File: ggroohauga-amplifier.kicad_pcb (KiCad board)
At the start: 2 copper layers, 95 x 31 mm, 12 parts

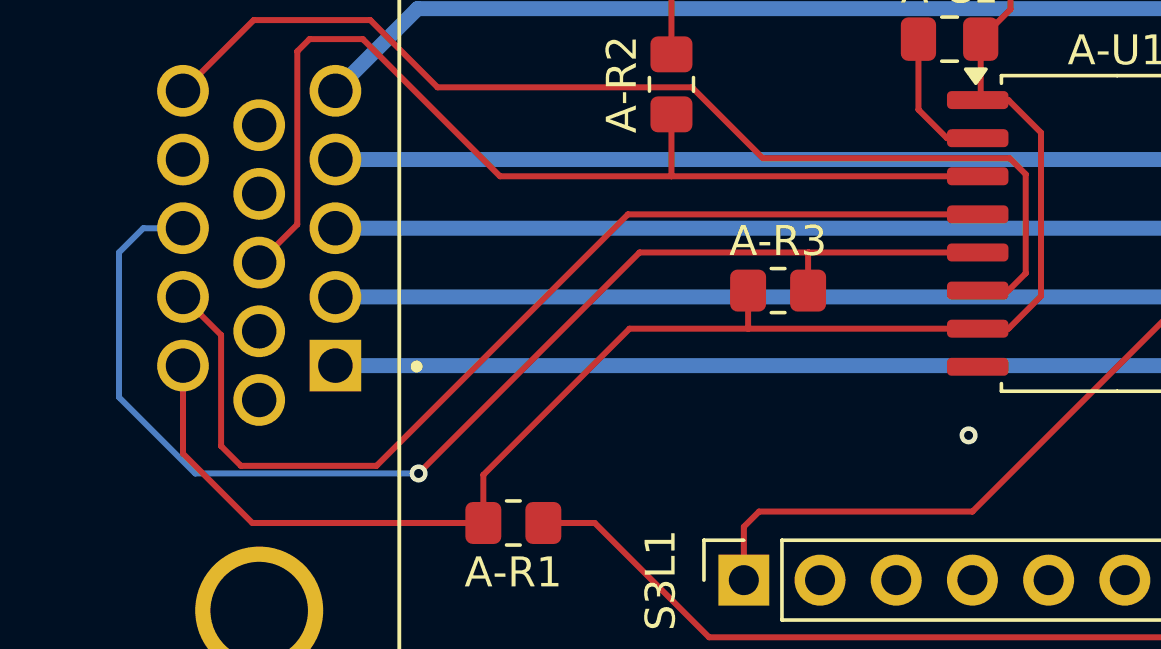
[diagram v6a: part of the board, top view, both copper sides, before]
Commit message: Move pull-up from AMP_RX to AMP_TX
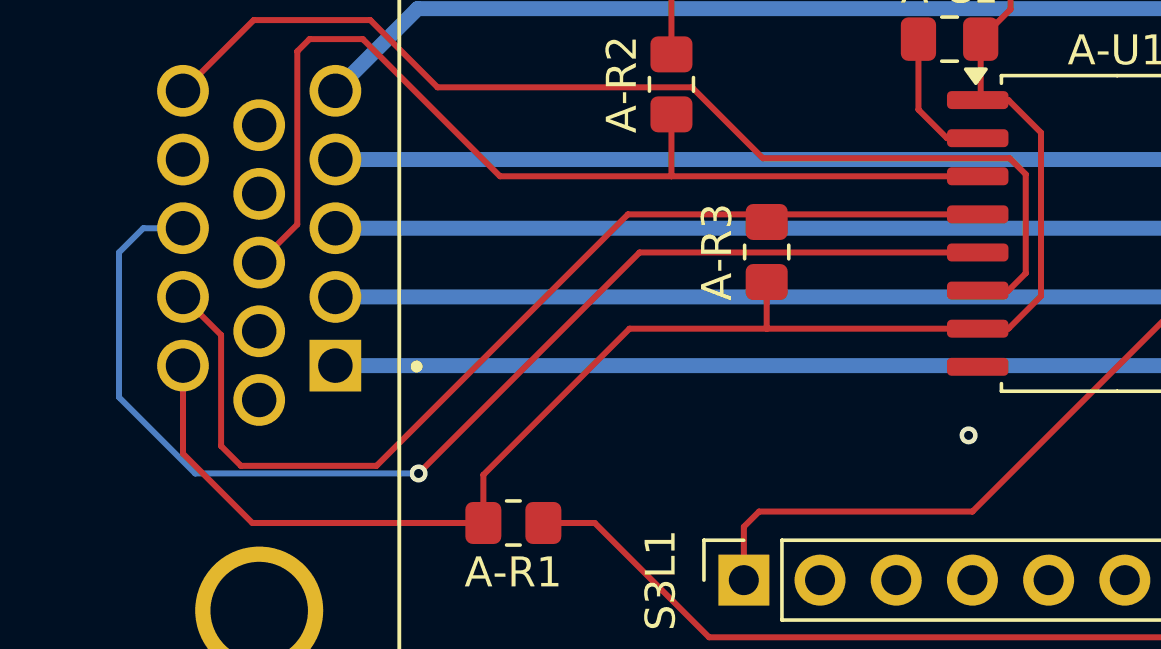
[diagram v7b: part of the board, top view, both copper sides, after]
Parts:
- moved A-R3 1.34 mm to (82.3, 66.5), turned to 90 degrees
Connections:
- A-R3 pad 2: /Common/AMP_RX -> /Common/AMP_TX
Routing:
- net /Common/AMP_RX: track 41.3 -> 40.0 mm
- net /Common/AMP_TX: track 34.5 -> 34.0 mm
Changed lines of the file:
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@@
 	(footprint "Resistor_SMD:R_0805_2012Metric_Pad1.20x1.40mm_HandSolder"
 		(layer "F.Cu")
-		(at 82.677 67.818)
+		(at 82.296 66.532 90)
 		(descr "Resistor SMD 0805 (2012 Metric), square (rectangular) end terminal, IPC-7351 nominal with elongated pad for handsoldering. (Body size source: IPC-SM-782 page 72, https://www.pcb-3d.com/wordpress/wp-content/uploads/ipc-sm-782a_amendment_1_and_2.pdf), generated with kicad-footprint-generator")
 		(tags "resistor handsolder")
 		(property "Reference" "A-R3"
-			(at 0 -1.65 0)
+			(at 0 -1.65 90)
 			(layer "F.SilkS")
 			(effects
@@
 		)
 		(property "Value" "10kΩ"
-			(at 0 1.65 0)
+			(at 0 1.65 90)
 			(layer "F.Fab")
 			(effects
@@
 		)
 		(property "Datasheet" ""
-			(at 0 0 0)
+			(at 0 0 90)
 			(layer "F.Fab")
 			(hide yes)
@@
 		)
 		(property "Description" "Resistor"
-			(at 0 0 0)
+			(at 0 0 90)
 			(layer "F.Fab")
 			(hide yes)
@@
 		)
 		(fp_line
-			(start -1.85 -0.95)
-			(end 1.85 -0.95)
+			(start 1.85 -0.95)
+			(end 1.85 0.95)
 			(stroke
 				(width 0.05)
@@
 		)
 		(fp_line
-			(start -1.85 0.95)
-			(end -1.85 -0.95)
+			(start -1.85 -0.95)
+			(end 1.85 -0.95)
 			(stroke
 				(width 0.05)
@@
 		)
 		(fp_line
-			(start 1.85 -0.95)
-			(end 1.85 0.95)
+			(start 1.85 0.95)
+			(end -1.85 0.95)
 			(stroke
 				(width 0.05)
@@
 		)
 		(fp_line
-			(start 1.85 0.95)
-			(end -1.85 0.95)
+			(start -1.85 0.95)
+			(end -1.85 -0.95)
 			(stroke
 				(width 0.05)
@@
 		)
 		(fp_line
-			(start -1 -0.625)
-			(end 1 -0.625)
+			(start 1 -0.625)
+			(end 1 0.625)
 			(stroke
 				(width 0.1)
@@
 		)
 		(fp_line
-			(start -1 0.625)
-			(end -1 -0.625)
+			(start -1 -0.625)
+			(end 1 -0.625)
 			(stroke
 				(width 0.1)
@@
 		)
 		(fp_line
-			(start 1 -0.625)
-			(end 1 0.625)
+			(start 1 0.625)
+			(end -1 0.625)
 			(stroke
 				(width 0.1)
@@
 		)
 		(fp_line
-			(start 1 0.625)
-			(end -1 0.625)
+			(start -1 0.625)
+			(end -1 -0.625)
 			(stroke
 				(width 0.1)
@@
 		)
 		(fp_text user "${REFERENCE}"
-			(at 0 0 0)
+			(at 0 0 90)
 			(layer "F.Fab")
 			(effects
@@
 		)
 		(pad "1" smd roundrect
-			(at -1 0)
+			(at -1 0 90)
 			(size 1.2 1.4)
 			(layers "F.Cu" "F.Mask" "F.Paste")
@@
 		)
 		(pad "2" smd roundrect
-			(at 1 0)
+			(at 1 0 90)
 			(size 1.2 1.4)
 			(layers "F.Cu" "F.Mask" "F.Paste")
 			(roundrect_rratio 0.208333)
-			(net 6 "/Common/AMP_RX")
+			(net 5 "/Common/AMP_TX")
 			(pintype "passive")
 		)
@@
 	)
 	(segment
-		(start 81.6864 69.088)
-		(end 77.724 69.088)
+		(start 89.33 69.088)
+		(end 82.296 69.088)
 		(width 0.2)
 		(layer "F.Cu")
@@
 	)
 	(segment
-		(start 89.33 69.088)
-		(end 81.6864 69.088)
+		(start 77.724 69.088)
+		(end 82.296 69.088)
 		(width 0.2)
 		(layer "F.Cu")
@@
 	)
 	(segment
-		(start 81.677 67.818)
-		(end 81.677 69.0786)
+		(start 65.151 75.565)
+		(end 72.8516 75.565)
 		(width 0.2)
 		(layer "F.Cu")
@@
 	)
 	(segment
-		(start 65.151 75.565)
-		(end 72.8516 75.565)
+		(start 82.296 67.532)
+		(end 82.296 69.088)
 		(width 0.2)
 		(layer "F.Cu")
@@
 	)
 	(segment
-		(start 81.6864 69.088)
-		(end 81.677 69.0786)
-		(width 0.2)
-		(layer "F.Cu")
-		(net 3)
-	)
-	(segment
 		(start 91.44 62.553001)
 		(end 91.44 68.002999)
@@
 	)
 	(segment
-		(start 64.77 73.66)
+		(start 64.1096 69.2992)
 		(end 64.1096 72.9996)
 		(width 0.2)
@@
 	)
 	(segment
-		(start 64.1096 72.9996)
+		(start 62.8396 68.0292)
 		(end 64.1096 69.2992)
 		(width 0.2)
@@
 	(segment
 		(start 77.671018 65.278)
-		(end 69.289018 73.66)
+		(end 82.042 65.278)
 		(width 0.2)
 		(layer "F.Cu")
@@
 	)
 	(segment
-		(start 69.289018 73.66)
-		(end 64.77 73.66)
+		(start 64.77 73.66)
+		(end 69.289018 73.66)
 		(width 0.2)
 		(layer "F.Cu")
@@
 	)
 	(segment
-		(start 77.671018 65.278)
-		(end 89.33 65.278)
+		(start 69.289018 73.66)
+		(end 77.671018 65.278)
 		(width 0.2)
 		(layer "F.Cu")
@@
 	)
 	(segment
-		(start 64.1096 69.2992)
-		(end 62.8396 68.0292)
+		(start 89.33 65.278)
+		(end 82.55 65.278)
 		(width 0.2)
 		(layer "F.Cu")
@@
 	)
 	(segment
-		(start 83.677 66.564)
-		(end 83.693 66.548)
-		(width 0.2)
-		(layer "F.Cu")
-		(net 6)
-	)
-	(segment
-		(start 83.677 67.818)
-		(end 83.677 66.564)
-		(width 0.2)
-		(layer "F.Cu")
-		(net 6)
-	)
-	(segment
-		(start 83.693 66.548)
-		(end 78.0586 66.548)
+		(start 64.1096 72.9996)
+		(end 64.77 73.66)
 		(width 0.2)
 		(layer "F.Cu")
-		(net 6)
+		(net 5)
 	)
 	(segment
@@
 	)
 	(segment
-		(start 83.693 66.548)
+		(start 78.0586 66.548)
 		(end 89.33 66.548)
 		(width 0.2)

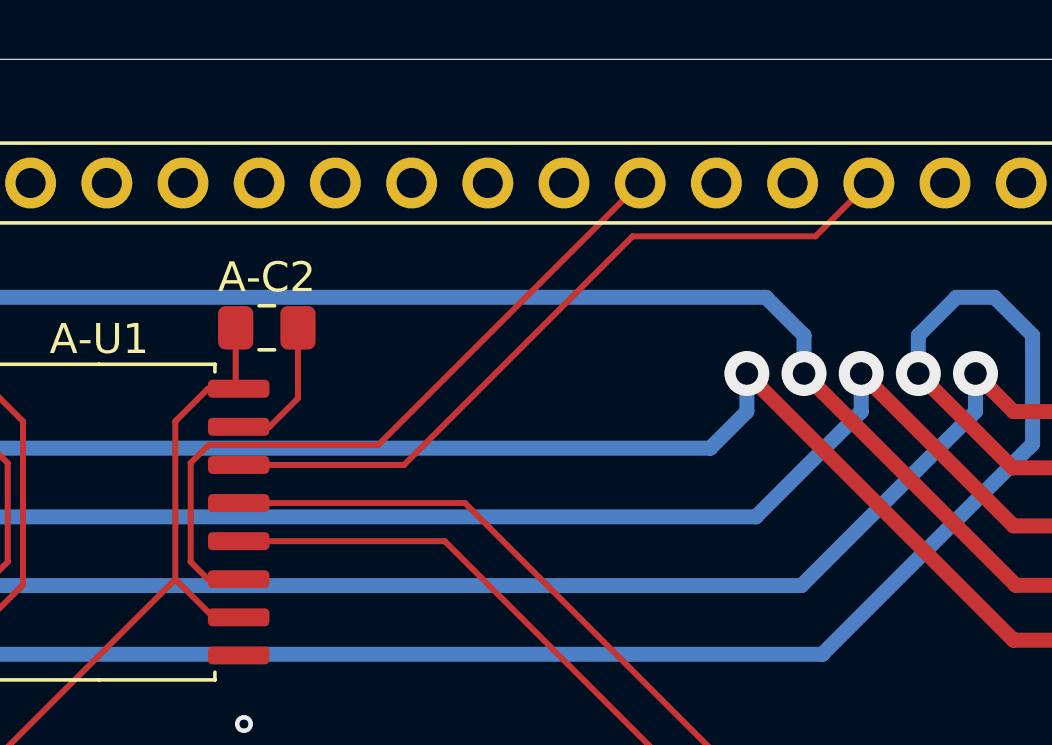
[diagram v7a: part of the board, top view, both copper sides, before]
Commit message: Fix GPIO assignments
Stop using GPIO 14 because the pull-up isn't working reliably on my LOLIN
S3 board even when floating and I don't have another one to test it with.

Don't use GPIO 35 on the DevKitC-1 board because that conflicts with the
Octal PSRAM.
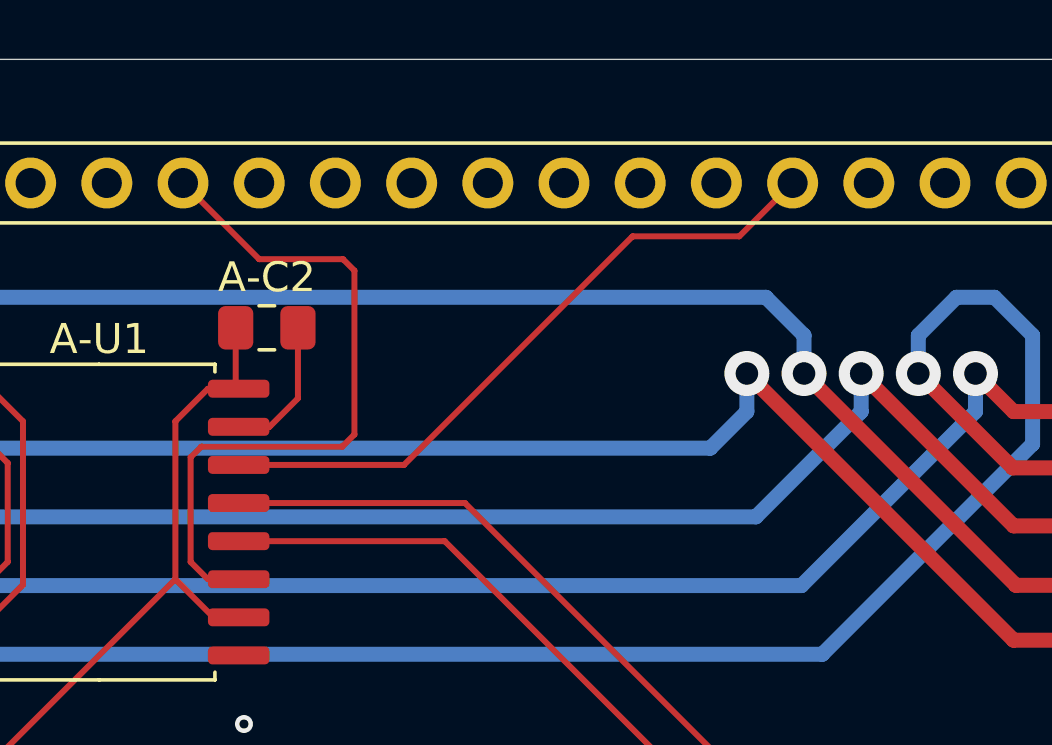
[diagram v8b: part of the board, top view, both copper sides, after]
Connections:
- A-U1 pad 11: /Common/GPIO_L48_C35_M36/CON_ANNOUNCE -> /Common/GPIO_L41_C41_M42/CON_ANNOUNCE
- A-U1 pad 14: /Common/GPIO_L14_C48_M33/AMP_DETECT -> /Common/GPIO_L21_C21_M21/AMP_DETECT
- S3R1 pad 13: /Common/GPIO_L48_C35_M36/CON_ANNOUNCE -> unconnected-(S3R1-Pin_13-Pad13)
- S3R1 pad 14: GND -> unconnected-(S3R1-Pin_14-Pad14)
- S3R1 pad 15: GND -> /Common/GPIO_L21_C21_M21/AMP_DETECT
- S3R1 pad 16: /Common/GPIO_L14_C48_M33/AMP_DETECT -> GND
- S3R1 pad 7: GND -> /Common/GPIO_L41_C41_M42/CON_ANNOUNCE
- S3R1 pad 9: GND -> unconnected-(S3R1-Pin_9-Pad9)
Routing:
- net /Common/GPIO_L14_C48_M33/AMP_DETECT: track 24.9 -> 0.00 mm
- net /Common/GPIO_L48_C35_M36/CON_ANNOUNCE: track 24.0 -> 0.00 mm
- net /Common/GPIO_L41_C41_M42/CON_ANNOUNCE: track 0.00 -> 23.5 mm
- net /Common/GPIO_L21_C21_M21/AMP_DETECT: track 0.00 -> 22.4 mm
